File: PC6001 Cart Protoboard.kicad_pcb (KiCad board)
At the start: 2 copper layers, 107.3 x 80.6 mm, 29 parts, among them J1 PC-6001 edge connector, SW1 PicoReset, SW2 EspReset, SW3 Button A, U2 ESP32-DevKitC, U3 74LS32, U4 microSD-Breakout, U5 74LS00, U6 SN74LVC245AN, U7 SN74LVC245AN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

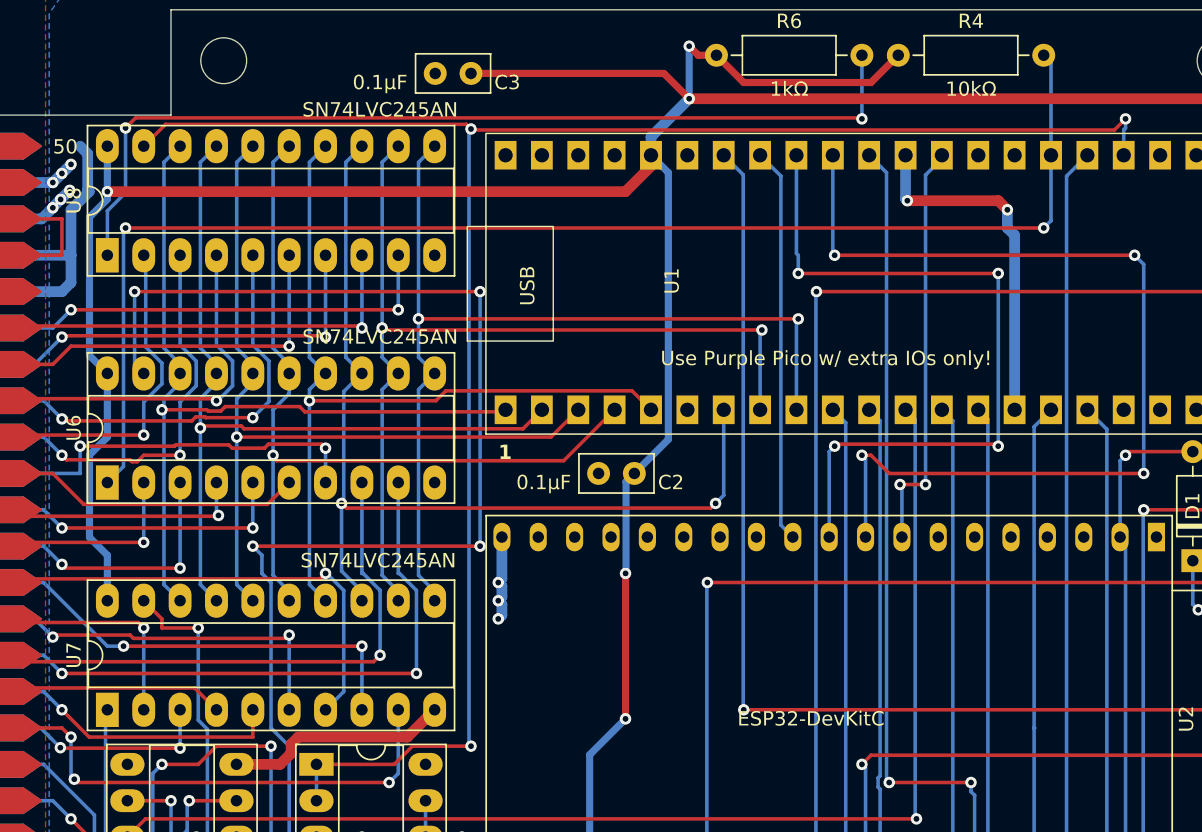
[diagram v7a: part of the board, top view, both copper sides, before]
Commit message: Fixing unrouted errors
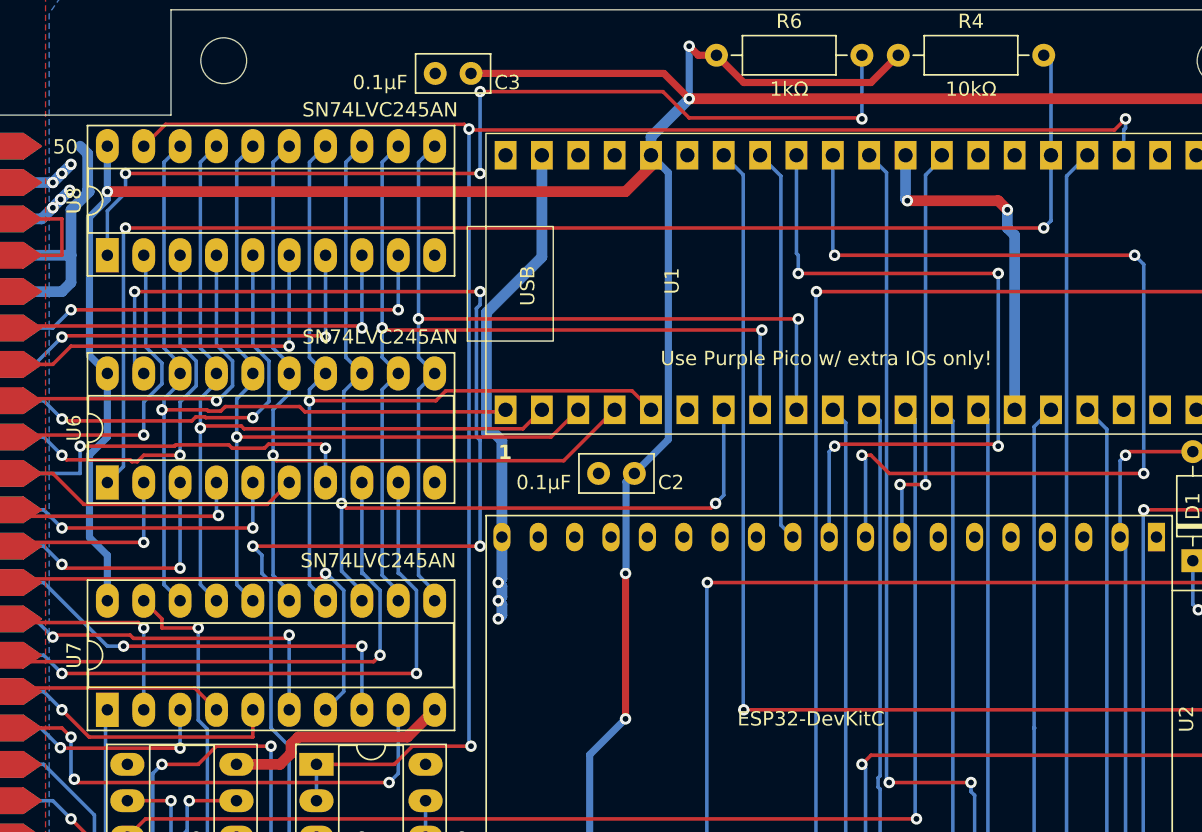
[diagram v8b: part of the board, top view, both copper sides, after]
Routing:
- net +5V: track 41.2 -> 70.2 mm
- net Net-(U8-DIR): track 65.6 -> 68.6 mm, vias 2 -> 4
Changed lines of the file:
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@@
 	)
 	(segment
+		(start 164.719 105.41)
+		(end 164.719 98.679)
+		(width 0.75)
+		(layer "B.Cu")
+		(net 40)
+	)
+	(segment
 		(start 133.35 82.37043)
 		(end 133.35 82.41)
@@
 	)
 	(segment
+		(start 164.135 98.095)
+		(end 163.636 98.095)
+		(width 0.75)
+		(layer "B.Cu")
+		(net 40)
+	)
+	(segment
 		(start 164.465 108.585)
 		(end 164.719 108.839)
@@
 	)
 	(segment
+		(start 163.636 98.095)
+		(end 163.636 89.729)
+		(width 0.75)
+		(layer "B.Cu")
+		(net 40)
+	)
+	(segment
 		(start 132.575 83.185)
 		(end 133.35 82.41)
@@
 	)
 	(segment
+		(start 163.636 89.729)
+		(end 167.513 85.852)
+		(width 0.75)
+		(layer "B.Cu")
+		(net 40)
+	)
+	(segment
 		(start 164.719 110.109)
 		(end 164.719 110.871)
@@
 	)
 	(segment
+		(start 167.513 85.852)
+		(end 167.513 78.74)
+		(width 0.75)
+		(layer "B.Cu")
+		(net 40)
+	)
+	(segment
 		(start 123.825 83.185)
 		(end 132.575 83.185)
@@
 	)
 	(segment
+		(start 164.719 98.679)
+		(end 164.135 98.095)
+		(width 0.75)
+		(layer "B.Cu")
+		(net 40)
+	)
+	(segment
 		(start 133.985 118.745)
 		(end 134.62 119.38)
@@
 	)
 	(segment
-		(start 135.91 88.265)
+		(start 135.91 92.73)
 		(end 135.91 83.061726)
 		(width 0.5)
@@
 	)
 	(segment
-		(start 135.91 92.73)
-		(end 135.91 88.265)
-		(width 0.5)
-		(layer "B.Cu")
-		(net 83)
-	)
-	(segment
 		(start 213.36 110.49)
 		(end 224.79 110.49)
@@
 	)
 	(segment
-		(start 207.505 76.975)
-		(end 162.63 76.975)
+		(start 151.765 121.285)
+		(end 157.19995 121.285)
 		(width 0.25)
 		(layer "F.Cu")
@@
 	)
 	(segment
-		(start 208.28 76.2)
-		(end 207.505 76.975)
+		(start 139.7 78.105)
+		(end 141.225 76.58)
 		(width 0.25)
 		(layer "F.Cu")
@@
 	)
 	(segment
-		(start 151.765 121.285)
-		(end 157.19995 121.285)
+		(start 141.225 76.58)
+		(end 162.095 76.58)
 		(width 0.25)
 		(layer "F.Cu")
@@
 	)
 	(segment
-		(start 162.63 76.975)
-		(end 162.56 76.905)
+		(start 207.505 76.975)
+		(end 162.49 76.975)
 		(width 0.25)
 		(layer "F.Cu")
@@
 	)
 	(segment
-		(start 158.46995 120.015)
-		(end 162.56 120.015)
+		(start 162.095 76.58)
+		(end 162.42 76.905)
 		(width 0.25)
 		(layer "F.Cu")
@@
 	)
 	(segment
-		(start 139.7 78.105)
-		(end 141.225 76.58)
+		(start 158.46995 120.015)
+		(end 162.56 120.015)
 		(width 0.25)
 		(layer "F.Cu")
@@
 	)
 	(segment
-		(start 162.235 76.58)
-		(end 162.56 76.905)
+		(start 162.49 76.975)
+		(end 162.42 76.905)
 		(width 0.25)
 		(layer "F.Cu")
@@
 	)
 	(segment
-		(start 141.225 76.58)
-		(end 162.235 76.58)
+		(start 208.28 76.2)
+		(end 207.505 76.975)
 		(width 0.25)
 		(layer "F.Cu")
@@
 	)
 	(via
-		(at 162.56 76.905)
+		(at 162.42 76.905)
 		(size 0.8)
 		(drill 0.4)
@@
 	(segment
 		(start 162.42 119.875)
-		(end 162.42 77.045)
+		(end 162.42 76.905)
 		(width 0.25)
 		(layer "B.Cu")
@@
 	)
 	(segment
-		(start 162.42 77.045)
-		(end 162.56 76.905)
-		(width 0.25)
-		(layer "B.Cu")
-		(net 97)
-	)
-	(segment
 		(start 208.28 76.2)
 		(end 208.28 76.835)
@@
 	)
 	(segment
-		(start 162.56 120.015)
-		(end 162.42 119.875)
+		(start 151.765 123.825)
+		(end 151.765 121.285)
 		(width 0.25)
 		(layer "B.Cu")
@@
 	)
 	(segment
-		(start 151.765 123.825)
-		(end 151.765 121.285)
+		(start 162.56 120.015)
+		(end 162.42 119.875)
 		(width 0.25)
 		(layer "B.Cu")
@@
 	)
 	(segment
-		(start 163.195 106.045)
-		(end 163.195 88.265)
+		(start 149.86 120.015)
+		(end 148.59 118.745)
 		(width 0.25)
 		(layer "B.Cu")
@@
 	)
 	(segment
-		(start 149.86 120.015)
-		(end 148.59 118.745)
+		(start 163.195 89.180051)
+		(end 163.195 88.265)
 		(width 0.25)
 		(layer "B.Cu")
@@
 	)
 	(segment
+		(start 163.195 98.643949)
+		(end 162.936 98.384949)
+		(width 0.25)
+		(layer "B.Cu")
+		(net 105)
+	)
+	(segment
+		(start 162.936 98.384949)
+		(end 162.936 89.43905)
+		(width 0.25)
+		(layer "B.Cu")
+		(net 105)
+	)
+	(segment
+		(start 163.195 106.045)
+		(end 163.195 98.643949)
+		(width 0.25)
+		(layer "B.Cu")
+		(net 105)
+	)
+	(segment
+		(start 162.936 89.43905)
+		(end 163.195 89.180051)
+		(width 0.25)
+		(layer "B.Cu")
+		(net 105)
+	)
+	(segment
 		(start 139.065 93.345)
 		(end 139.7 93.98)
@@
 	)
 	(segment
-		(start 139.135 76.13)
-		(end 189.795 76.13)
+		(start 163.195 74.295)
+		(end 175.965 74.295)
 		(width 0.25)
 		(layer "F.Cu")
@@
 	)
 	(segment
-		(start 138.43 76.835)
-		(end 139.135 76.13)
+		(start 138.43 80.01)
+		(end 163.195 80.01)
 		(width 0.25)
 		(layer "F.Cu")
 		(net 120)
 	)
+	(segment
+		(start 177.8 76.13)
+		(end 189.795 76.13)
+		(width 0.25)
+		(layer "F.Cu")
+		(net 120)
+	)
+	(segment
+		(start 175.965 74.295)
+		(end 177.8 76.13)
+		(width 0.25)
+		(layer "F.Cu")
+		(net 120)
+	)
+	(via
+		(at 163.195 74.295)
+		(size 0.8)
+		(drill 0.4)
+		(layers "F.Cu" "B.Cu")
+		(net 120)
+	)
+	(via
+		(at 163.195 80.01)
+		(size 0.8)
+		(drill 0.4)
+		(layers "F.Cu" "B.Cu")
+		(net 120)
+	)
 	(via
 		(at 189.865 76.2)
@@
 	)
 	(via
-		(at 138.43 76.835)
+		(at 138.43 80.01)
 		(size 0.8)
 		(drill 0.4)
@@
 	)
 	(segment
-		(start 189.865 76.2)
-		(end 189.865 71.755)
+		(start 138.43 81.354898)
+		(end 138.43 80.01)
 		(width 0.25)
 		(layer "B.Cu")
@@
 	)
 	(segment
-		(start 138.43 81.354898)
-		(end 138.43 76.835)
+		(start 163.195 80.01)
+		(end 163.195 74.295)
+		(width 0.25)
+		(layer "B.Cu")
+		(net 120)
+	)
+	(segment
+		(start 189.865 76.2)
+		(end 189.865 71.755)
 		(width 0.25)
 		(layer "B.Cu")
